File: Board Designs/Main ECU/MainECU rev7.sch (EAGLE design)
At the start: 202 parts, among them J1 JUMPER, J2 JUMPER, J3 JUMPER, J4 JUMPER, J5 JUMPER, J6 JUMPER, J7 JUMPER, J8 JUMPER, P1 SOLDER_PAD, P2 SOLDER_PAD, Q1 P-CHANNEL_MOSFET_DMP3099L-7, Q12 P-CHANNEL_MOSFET_DMP3099L-7, X1 CONNECTOR-37, X2 CONNECTOR-4AUTOSPORT, X3 CONNECTOR-4NANO-FIT-VERTICAL-4, X4 CONNECTOR-4NANO-FIT-VERTICAL-4

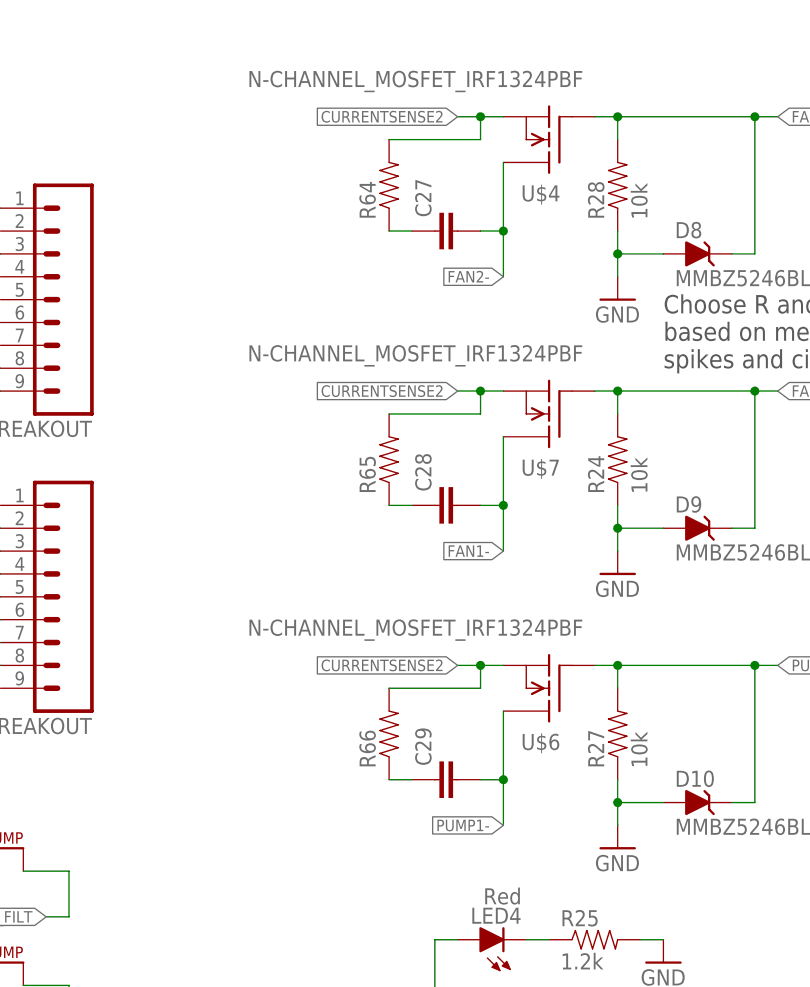
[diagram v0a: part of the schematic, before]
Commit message: Flipped Resistor and capacitor posistions
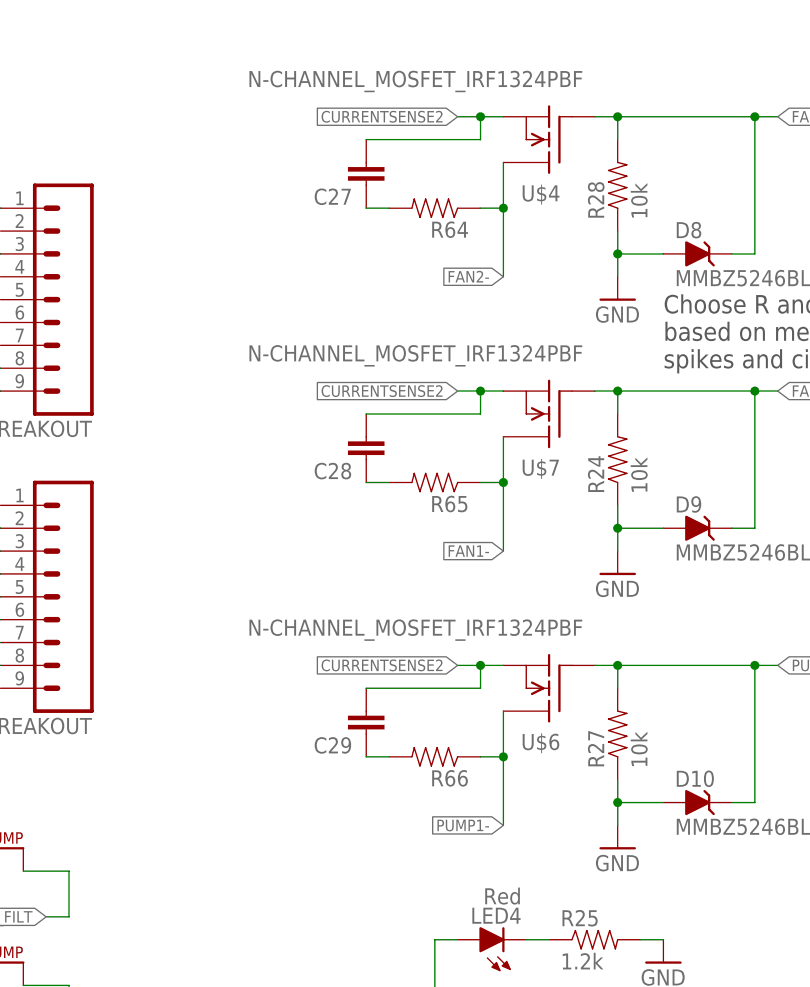
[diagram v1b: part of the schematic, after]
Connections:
- net CURRENTSENSE2: now also C27.2, C28.2, C29.2; no longer R64.2, R65.2, R66.2
- net FAN1-: now also R65.1; no longer C28.2
- net FAN2-: now also R64.1; no longer C27.2
- net N$65: now also R64.2; no longer R64.1
- net N$74: now also R65.2; no longer R65.1
- net N$75: now also R66.2; no longer R66.1
- net PUMP1-: now also R66.1; no longer C29.2
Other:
- moved on the sheet: C27, C28, C29, R64, R65, R66
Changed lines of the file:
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@@
 <instance part="P1" gate="G$1" x="373.38" y="111.76" smashed="yes"/>
 <instance part="P2" gate="G$1" x="373.38" y="119.38" smashed="yes"/>
-<instance part="R64" gate="G$1" x="553.72" y="254" smashed="yes" rot="R90">
-<attribute name="NAME" x="552.2214" y="250.19" size="1.778" layer="95" rot="R90"/>
-<attribute name="VALUE" x="557.022" y="250.19" size="1.778" layer="96" rot="R90"/>
+<instance part="R64" gate="G$1" x="558.8" y="251.46" smashed="yes" rot="R180">
+<attribute name="NAME" x="562.61" y="249.9614" size="1.778" layer="95" rot="R180"/>
+<attribute name="VALUE" x="562.61" y="254.762" size="1.778" layer="96" rot="R180"/>
 </instance>
-<instance part="C27" gate="G$1" x="561.34" y="248.92" smashed="yes" rot="R90">
-<attribute name="NAME" x="558.419" y="250.444" size="1.778" layer="95" rot="R90"/>
-<attribute name="VALUE" x="563.499" y="250.444" size="1.778" layer="96" rot="R90"/>
+<instance part="C27" gate="G$1" x="551.18" y="256.54" smashed="yes" rot="R180">
+<attribute name="NAME" x="549.656" y="253.619" size="1.778" layer="95" rot="R180"/>
+<attribute name="VALUE" x="549.656" y="258.699" size="1.778" layer="96" rot="R180"/>
 </instance>
-<instance part="R65" gate="G$1" x="553.72" y="223.52" smashed="yes" rot="R90">
-<attribute name="NAME" x="552.2214" y="219.71" size="1.778" layer="95" rot="R90"/>
-<attribute name="VALUE" x="557.022" y="219.71" size="1.778" layer="96" rot="R90"/>
+<instance part="R65" gate="G$1" x="558.8" y="220.98" smashed="yes" rot="R180">
+<attribute name="NAME" x="562.61" y="219.4814" size="1.778" layer="95" rot="R180"/>
+<attribute name="VALUE" x="562.61" y="224.282" size="1.778" layer="96" rot="R180"/>
 </instance>
-<instance part="C28" gate="G$1" x="561.34" y="218.44" smashed="yes" rot="R90">
-<attribute name="NAME" x="558.419" y="219.964" size="1.778" layer="95" rot="R90"/>
-<attribute name="VALUE" x="563.499" y="219.964" size="1.778" layer="96" rot="R90"/>
+<instance part="C28" gate="G$1" x="551.18" y="226.06" smashed="yes" rot="R180">
+<attribute name="NAME" x="549.656" y="223.139" size="1.778" layer="95" rot="R180"/>
+<attribute name="VALUE" x="549.656" y="228.219" size="1.778" layer="96" rot="R180"/>
 </instance>
-<instance part="R66" gate="G$1" x="553.72" y="193.04" smashed="yes" rot="R90">
-<attribute name="NAME" x="552.2214" y="189.23" size="1.778" layer="95" rot="R90"/>
-<attribute name="VALUE" x="557.022" y="189.23" size="1.778" layer="96" rot="R90"/>
+<instance part="R66" gate="G$1" x="558.8" y="190.5" smashed="yes" rot="R180">
+<attribute name="NAME" x="562.61" y="189.0014" size="1.778" layer="95" rot="R180"/>
+<attribute name="VALUE" x="562.61" y="193.802" size="1.778" layer="96" rot="R180"/>
 </instance>
-<instance part="C29" gate="G$1" x="561.34" y="187.96" smashed="yes" rot="R90">
-<attribute name="NAME" x="558.419" y="189.484" size="1.778" layer="95" rot="R90"/>
-<attribute name="VALUE" x="563.499" y="189.484" size="1.778" layer="96" rot="R90"/>
+<instance part="C29" gate="G$1" x="551.18" y="195.58" smashed="yes" rot="R180">
+<attribute name="NAME" x="549.656" y="192.659" size="1.778" layer="95" rot="R180"/>
+<attribute name="VALUE" x="549.656" y="197.739" size="1.778" layer="96" rot="R180"/>
 </instance>
 </instances>
@@
 <net name="PUMP1-" class="0">
 <segment>
-<wire x1="566.42" y1="182.88" x2="566.42" y2="187.96" width="0.1524" layer="91"/>
 <label x="566.42" y="182.88" size="1.27" layer="95" rot="R180" xref="yes"/>
 <pinref part="U$6" gate="G$1" pin="D"/>
-<pinref part="C29" gate="G$1" pin="2"/>
-<wire x1="566.42" y1="187.96" x2="566.42" y2="195.58" width="0.1524" layer="91"/>
-<wire x1="563.88" y1="187.96" x2="566.42" y2="187.96" width="0.1524" layer="91"/>
-<junction x="566.42" y="187.96"/>
+<wire x1="566.42" y1="182.88" x2="566.42" y2="190.5" width="0.1524" layer="91"/>
+<pinref part="R66" gate="G$1" pin="1"/>
+<wire x1="566.42" y1="190.5" x2="566.42" y2="195.58" width="0.1524" layer="91"/>
+<wire x1="563.88" y1="190.5" x2="566.42" y2="190.5" width="0.1524" layer="91"/>
+<junction x="566.42" y="190.5"/>
 </segment>
 <segment>
@@
 <label x="566.42" y="213.36" size="1.27" layer="95" rot="R180" xref="yes"/>
 <pinref part="U$7" gate="G$1" pin="D"/>
-<wire x1="566.42" y1="226.06" x2="566.42" y2="218.44" width="0.1524" layer="91"/>
-<pinref part="C28" gate="G$1" pin="2"/>
-<wire x1="566.42" y1="218.44" x2="566.42" y2="213.36" width="0.1524" layer="91"/>
-<wire x1="563.88" y1="218.44" x2="566.42" y2="218.44" width="0.1524" layer="91"/>
-<junction x="566.42" y="218.44"/>
+<wire x1="566.42" y1="226.06" x2="566.42" y2="220.98" width="0.1524" layer="91"/>
+<pinref part="R65" gate="G$1" pin="1"/>
+<wire x1="566.42" y1="220.98" x2="566.42" y2="213.36" width="0.1524" layer="91"/>
+<wire x1="563.88" y1="220.98" x2="566.42" y2="220.98" width="0.1524" layer="91"/>
+<junction x="566.42" y="220.98"/>
 </segment>
 <segment>
@@
 <net name="FAN2-" class="0">
 <segment>
-<wire x1="566.42" y1="243.84" x2="566.42" y2="248.92" width="0.1524" layer="91"/>
 <label x="566.42" y="243.84" size="1.27" layer="95" rot="R180" xref="yes"/>
 <pinref part="U$4" gate="G$1" pin="D"/>
-<pinref part="C27" gate="G$1" pin="2"/>
-<wire x1="566.42" y1="248.92" x2="566.42" y2="256.54" width="0.1524" layer="91"/>
-<wire x1="563.88" y1="248.92" x2="566.42" y2="248.92" width="0.1524" layer="91"/>
-<junction x="566.42" y="248.92"/>
+<wire x1="566.42" y1="243.84" x2="566.42" y2="251.46" width="0.1524" layer="91"/>
+<pinref part="R64" gate="G$1" pin="1"/>
+<wire x1="566.42" y1="251.46" x2="566.42" y2="256.54" width="0.1524" layer="91"/>
+<wire x1="566.42" y1="251.46" x2="563.88" y2="251.46" width="0.1524" layer="91"/>
+<junction x="566.42" y="251.46"/>
 </segment>
 <segment>
@@
 <net name="CURRENTSENSE2" class="0">
 <segment>
-<wire x1="566.42" y1="261.62" x2="563.88" y2="261.62" width="0.1524" layer="91"/>
 <label x="561.34" y="261.62" size="1.27" layer="95" rot="R180" xref="yes"/>
 <pinref part="U$4" gate="G$1" pin="S"/>
+<wire x1="566.42" y1="261.62" x2="563.88" y2="261.62" width="0.1524" layer="91"/>
 <wire x1="563.88" y1="261.62" x2="561.34" y2="261.62" width="0.1524" layer="91"/>
 <wire x1="563.88" y1="261.62" x2="563.88" y2="259.08" width="0.1524" layer="91"/>
 <junction x="563.88" y="261.62"/>
-<pinref part="R64" gate="G$1" pin="2"/>
-<wire x1="563.88" y1="259.08" x2="553.72" y2="259.08" width="0.1524" layer="91"/>
+<pinref part="C27" gate="G$1" pin="2"/>
+<wire x1="563.88" y1="259.08" x2="551.18" y2="259.08" width="0.1524" layer="91"/>
 </segment>
 <segment>
-<wire x1="561.34" y1="231.14" x2="563.88" y2="231.14" width="0.1524" layer="91"/>
 <label x="561.34" y="231.14" size="1.27" layer="95" rot="R180" xref="yes"/>
 <pinref part="U$7" gate="G$1" pin="S"/>
-<pinref part="R65" gate="G$1" pin="2"/>
+<wire x1="561.34" y1="231.14" x2="563.88" y2="231.14" width="0.1524" layer="91"/>
+<pinref part="C28" gate="G$1" pin="2"/>
 <wire x1="563.88" y1="231.14" x2="566.42" y2="231.14" width="0.1524" layer="91"/>
-<wire x1="553.72" y1="228.6" x2="563.88" y2="228.6" width="0.1524" layer="91"/>
-<wire x1="563.88" y1="228.6" x2="563.88" y2="231.14" width="0.1524" layer="91"/>
+<wire x1="551.18" y1="228.6" x2="563.88" y2="228.6" width="0.1524" layer="91"/>
+<wire x1="563.88" y1="231.14" x2="563.88" y2="228.6" width="0.1524" layer="91"/>
 <junction x="563.88" y="231.14"/>
 </segment>
 <segment>
-<wire x1="566.42" y1="200.66" x2="563.88" y2="200.66" width="0.1524" layer="91"/>
 <label x="561.34" y="200.66" size="1.27" layer="95" rot="R180" xref="yes"/>
 <pinref part="U$6" gate="G$1" pin="S"/>
-<pinref part="R66" gate="G$1" pin="2"/>
+<wire x1="566.42" y1="200.66" x2="563.88" y2="200.66" width="0.1524" layer="91"/>
 <wire x1="563.88" y1="200.66" x2="561.34" y2="200.66" width="0.1524" layer="91"/>
-<wire x1="553.72" y1="198.12" x2="563.88" y2="198.12" width="0.1524" layer="91"/>
-<wire x1="563.88" y1="198.12" x2="563.88" y2="200.66" width="0.1524" layer="91"/>
+<wire x1="563.88" y1="200.66" x2="563.88" y2="198.12" width="0.1524" layer="91"/>
 <junction x="563.88" y="200.66"/>
+<pinref part="C29" gate="G$1" pin="2"/>
+<wire x1="563.88" y1="198.12" x2="551.18" y2="198.12" width="0.1524" layer="91"/>
 </segment>
 <segment>
@@
 </segment>
 </net>
-<net name="N$65" class="0">
+<net name="N$74" class="0">
 <segment>
-<pinref part="R64" gate="G$1" pin="1"/>
-<pinref part="C27" gate="G$1" pin="1"/>
-<wire x1="553.72" y1="248.92" x2="556.26" y2="248.92" width="0.1524" layer="91"/>
+<pinref part="R65" gate="G$1" pin="2"/>
+<pinref part="C28" gate="G$1" pin="1"/>
+<wire x1="553.72" y1="220.98" x2="551.18" y2="220.98" width="0.1524" layer="91"/>
 </segment>
 </net>
-<net name="N$74" class="0">
+<net name="N$65" class="0">
 <segment>
-<pinref part="R65" gate="G$1" pin="1"/>
-<pinref part="C28" gate="G$1" pin="1"/>
-<wire x1="553.72" y1="218.44" x2="556.26" y2="218.44" width="0.1524" layer="91"/>
+<pinref part="R64" gate="G$1" pin="2"/>
+<pinref part="C27" gate="G$1" pin="1"/>
+<wire x1="553.72" y1="251.46" x2="551.18" y2="251.46" width="0.1524" layer="91"/>
 </segment>
 </net>
 <net name="N$75" class="0">
 <segment>
+<pinref part="R66" gate="G$1" pin="2"/>
 <pinref part="C29" gate="G$1" pin="1"/>
-<pinref part="R66" gate="G$1" pin="1"/>
-<wire x1="556.26" y1="187.96" x2="553.72" y2="187.96" width="0.1524" layer="91"/>
+<wire x1="553.72" y1="190.5" x2="551.18" y2="190.5" width="0.1524" layer="91"/>
 </segment>
 </net>

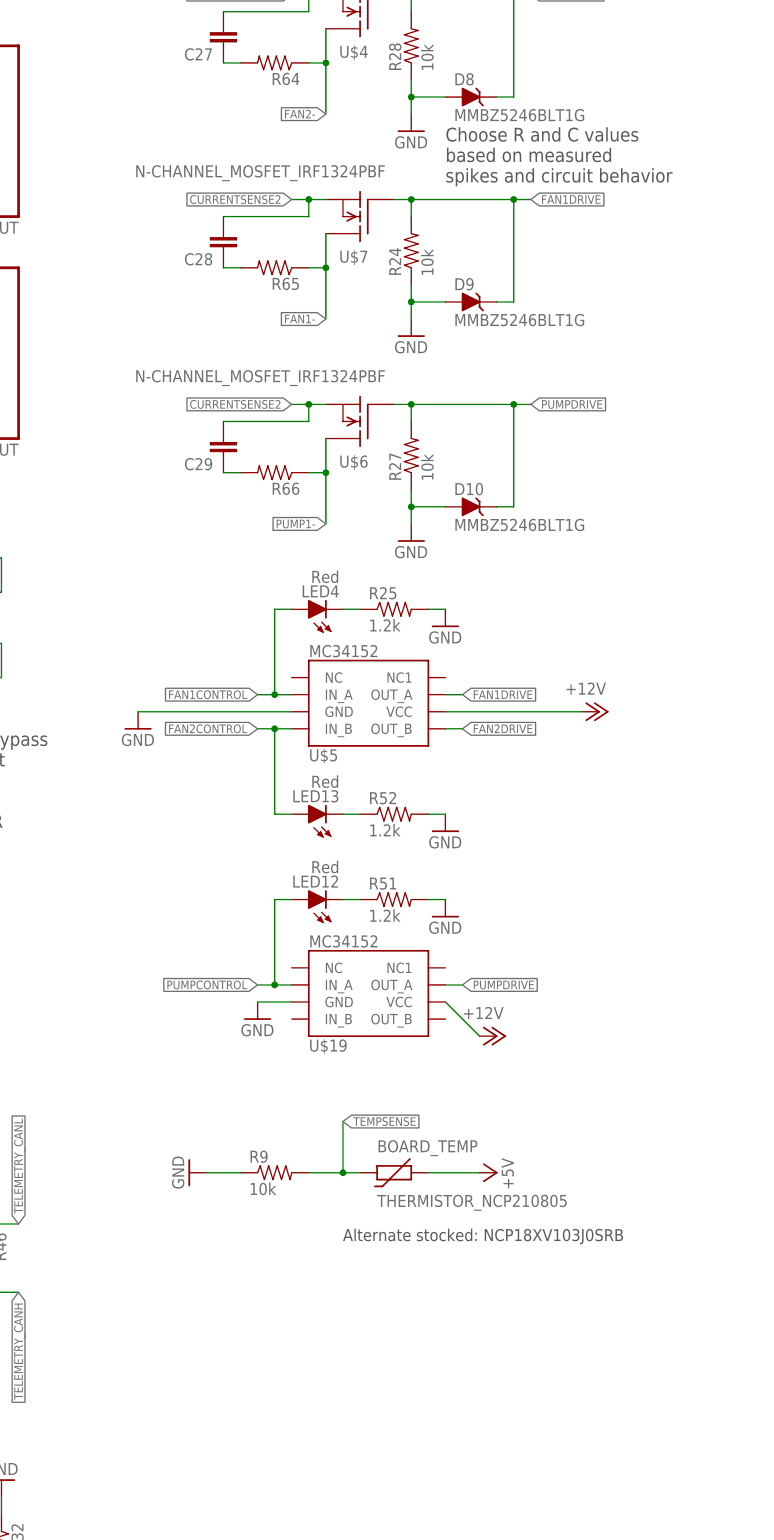
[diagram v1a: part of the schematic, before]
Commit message: Tweaks to RC snubber components and traces
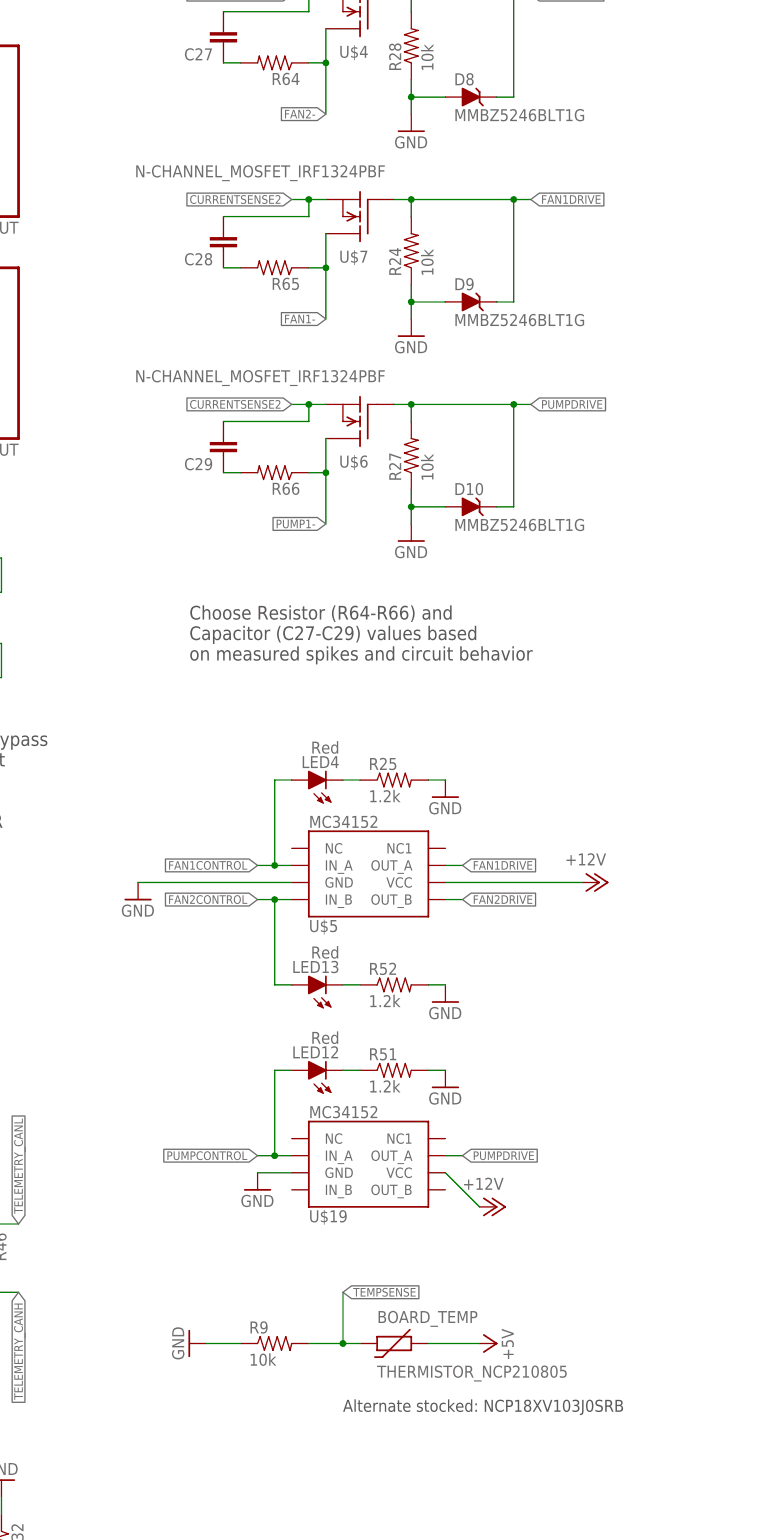
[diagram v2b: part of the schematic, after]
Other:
- note added: "Choose Resistor (R64-R66) and Capacitor (C27-C29) values based on measured spikes and circuit behavior"
- note removed: "Choose R and C values based on measured spikes and circuit behavior"
- moved on the sheet: BOARD_TEMP, LED12, LED13, LED4, R25, R51, R52, R9, U$19, U$5

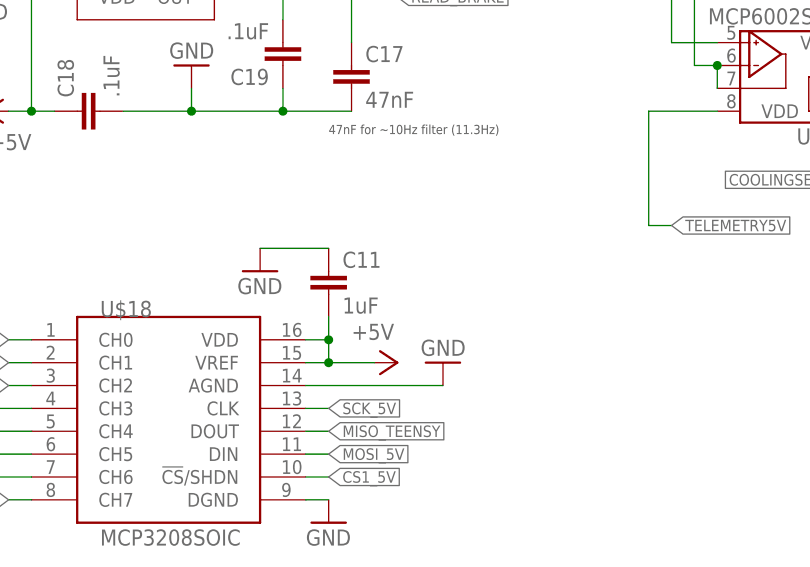
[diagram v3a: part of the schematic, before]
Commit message: Added second 0.1 capacitor and began moving traces
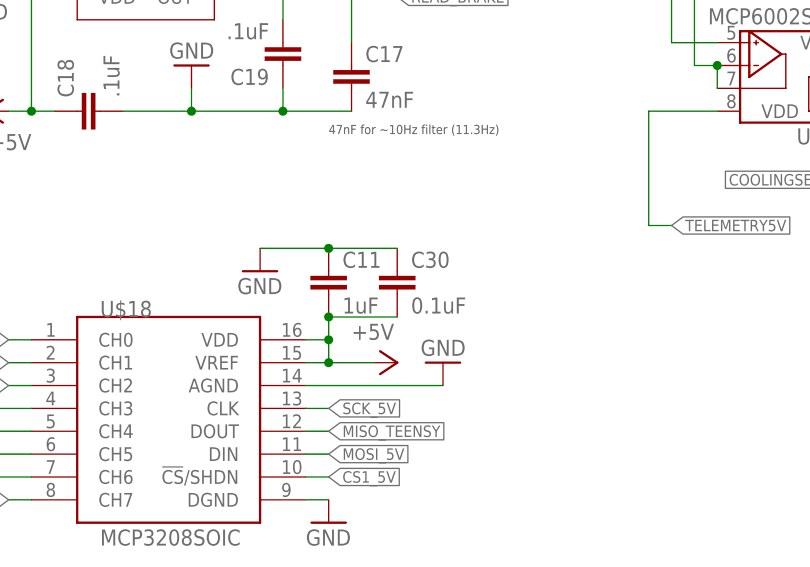
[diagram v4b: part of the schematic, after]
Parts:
- added C30: 0.1uF, HyTechDevices:CAP0805
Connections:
- net +5V: now also C30.2
- net GND: now also C30.1
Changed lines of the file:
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@@
 <?xml version="1.0" encoding="utf-8"?>
 <!DOCTYPE eagle SYSTEM "eagle.dtd">
-<eagle version="9.2.2">
+<eagle version="9.3.1">
 <drawing>
 <settings>
-<setting alwaysvectorfont="no"/>
+<setting alwaysvectorfont="yes"/>
 <setting verticaltext="up"/>
 </settings>
-<grid distance="0.1" unitdist="inch" unit="inch" style="lines" multiple="1" display="no" altdistance="0.01" altunitdist="inch" altunit="inch"/>
+<grid distance="0.1" unitdist="inch" unit="inch" style="lines" multiple="1" display="yes" altdistance="0.01" altunitdist="inch" altunit="inch"/>
 <layers>
 <layer number="1" name="Top" color="4" fill="1" visible="no" active="no"/>
@@
 <part name="R66" library="HyTechDevices" deviceset="RESISTOR" device="0805-RES"/>
 <part name="C29" library="HyTechDevices" deviceset="CAP" device="0805"/>
+<part name="C30" library="HyTechDevices" deviceset="CAP" device="0805" value="0.1uF"/>
 </parts>
 <sheets>
@@
 <attribute name="VALUE" x="549.656" y="197.739" size="1.778" layer="96" rot="R180"/>
 </instance>
+<instance part="C30" gate="G$1" x="365.76" y="154.94" smashed="yes">
+<attribute name="NAME" x="367.284" y="157.861" size="1.778" layer="95"/>
+<attribute name="VALUE" x="367.284" y="152.781" size="1.778" layer="96"/>
+</instance>
 </instances>
 <busses>
@@
 <pinref part="C11" gate="G$1" pin="1"/>
 <wire x1="358.14" y1="160.02" x2="350.52" y2="160.02" width="0.1524" layer="91"/>
+<pinref part="C30" gate="G$1" pin="1"/>
+<wire x1="365.76" y1="160.02" x2="358.14" y2="160.02" width="0.1524" layer="91"/>
+<junction x="358.14" y="160.02"/>
 </segment>
 <segment>
@@
 <wire x1="363.22" y1="147.32" x2="358.14" y2="147.32" width="0.1524" layer="91"/>
 <junction x="358.14" y="147.32"/>
-</segment>
-<segment>
+<pinref part="C30" gate="G$1" pin="2"/>
+<wire x1="358.14" y1="152.4" x2="365.76" y2="152.4" width="0.1524" layer="91"/>
+<junction x="358.14" y="152.4"/>
+</segment>
+<segment>
